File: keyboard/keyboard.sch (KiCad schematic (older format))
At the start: 23 parts, among them J1 Mini-DIN-6, J2 Conn_01x13, U1 74HC595, U2 74HC595, U3 74HC180, U4 74HC08, U5 74HC14

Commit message: Update keyboard
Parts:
- added C8: 1uF, Capacitor_THT:CP_Radial_D4.0mm_P2.00mm, symbol Device:CP
- H1, H2, H3, H4: footprint MountingHole:MountingHole_2.7mm_M2.5_Pad -> MountingHole:MountingHole_3.2mm_M3_Pad
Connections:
- net GND: now also C8.2
- net VCC: now also C8.1
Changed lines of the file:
@@
 F 0 "H1" V 9704 2450 50  0000 L CNN
 F 1 "MountingHole_Pad" V 9795 2450 50  0000 L CNN
-F 2 "MountingHole:MountingHole_2.7mm_M2.5_Pad" H 9750 2300 50  0001 C CNN
+F 2 "MountingHole:MountingHole_3.2mm_M3_Pad" H 9750 2300 50  0001 C CNN
 F 3 "~" H 9750 2300 50  0001 C CNN
 	1    9750 2300
@@
 F 0 "H2" V 9704 2650 50  0000 L CNN
 F 1 "MountingHole_Pad" V 9795 2650 50  0000 L CNN
-F 2 "MountingHole:MountingHole_2.7mm_M2.5_Pad" H 9750 2500 50  0001 C CNN
+F 2 "MountingHole:MountingHole_3.2mm_M3_Pad" H 9750 2500 50  0001 C CNN
 F 3 "~" H 9750 2500 50  0001 C CNN
 	1    9750 2500
@@
 F 0 "H3" V 9704 2850 50  0000 L CNN
 F 1 "MountingHole_Pad" V 9795 2850 50  0000 L CNN
-F 2 "MountingHole:MountingHole_2.7mm_M2.5_Pad" H 9750 2700 50  0001 C CNN
+F 2 "MountingHole:MountingHole_3.2mm_M3_Pad" H 9750 2700 50  0001 C CNN
 F 3 "~" H 9750 2700 50  0001 C CNN
 	1    9750 2700
@@
 F 0 "H4" V 9704 3050 50  0000 L CNN
 F 1 "MountingHole_Pad" V 9795 3050 50  0000 L CNN
-F 2 "MountingHole:MountingHole_2.7mm_M2.5_Pad" H 9750 2900 50  0001 C CNN
+F 2 "MountingHole:MountingHole_3.2mm_M3_Pad" H 9750 2900 50  0001 C CNN
 F 3 "~" H 9750 2900 50  0001 C CNN
 	1    9750 2900
@@
 	1    0    0    -1
 $EndComp
+$Comp
+L Device:CP C8
+U 1 1 60B22BE5
+P 4050 7150
+F 0 "C8" H 4168 7196 50  0000 L CNN
+F 1 "1uF" H 4168 7105 50  0000 L CNN
+F 2 "Capacitor_THT:CP_Radial_D4.0mm_P2.00mm" H 4088 7000 50  0001 C CNN
+F 3 "~" H 4050 7150 50  0001 C CNN
+	1    4050 7150
+	1    0    0    -1
+$EndComp
+Wire Wire Line
+	3550 7000 4050 7000
+Connection ~ 3550 7000
+Wire Wire Line
+	4050 7300 3550 7300
+Connection ~ 3550 7300
 Wire Bus Line
 	4900 5150 6800 5150

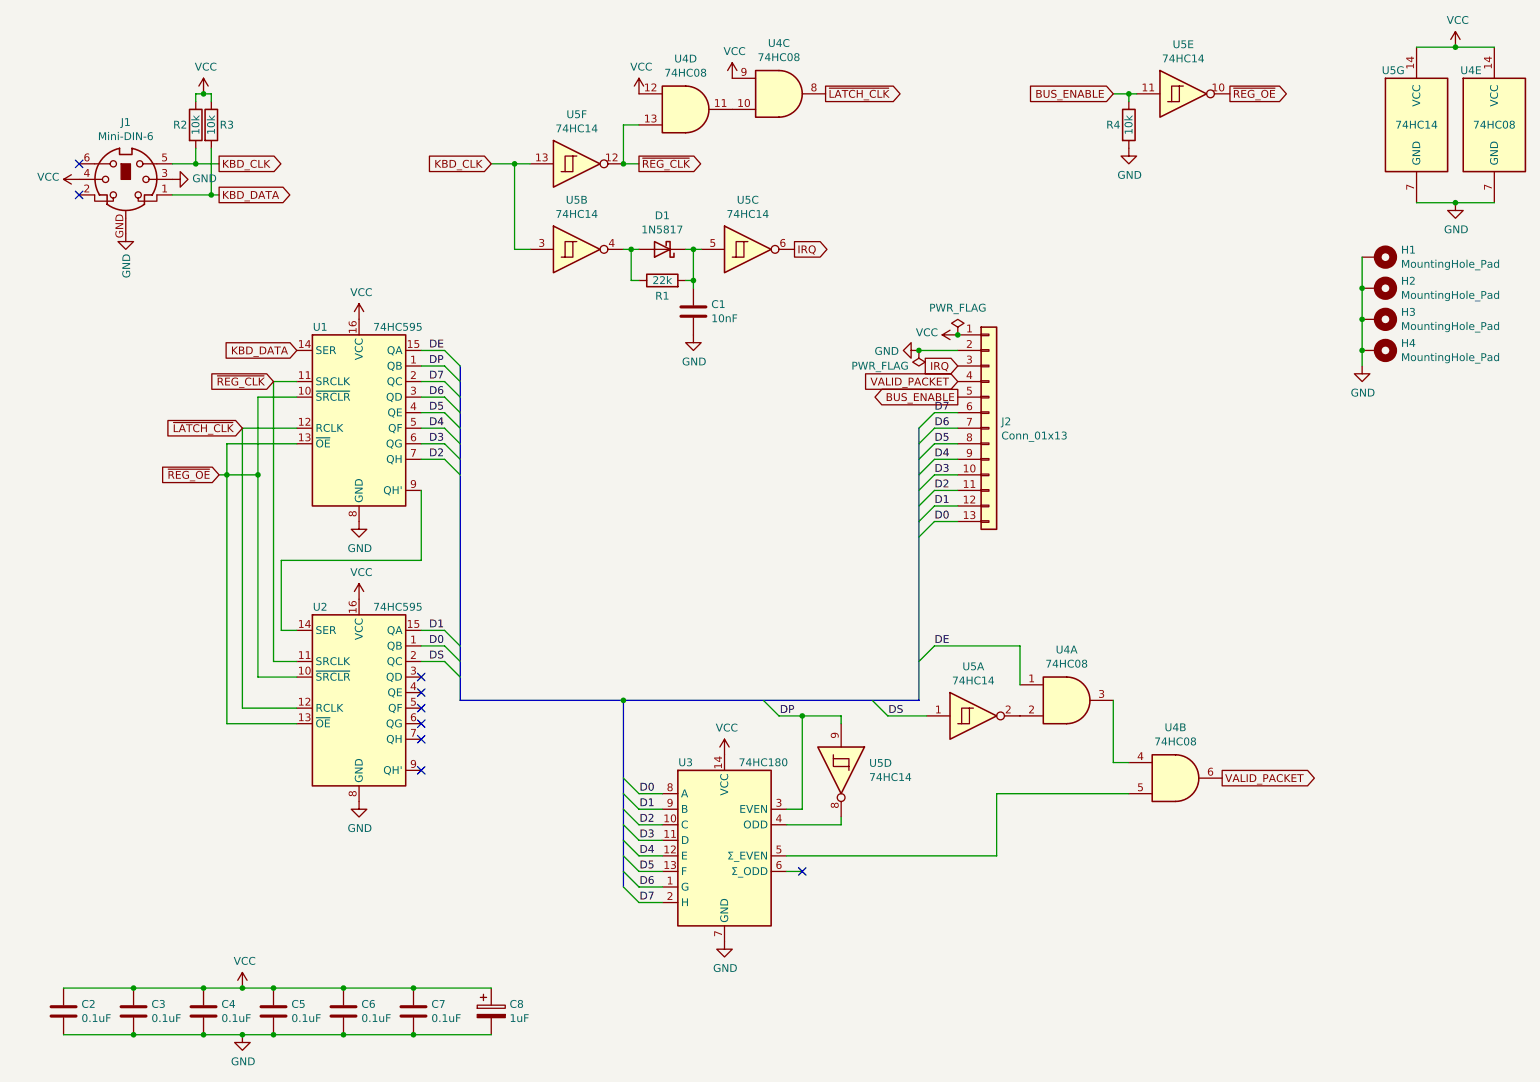
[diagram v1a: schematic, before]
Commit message: Updated keyboard
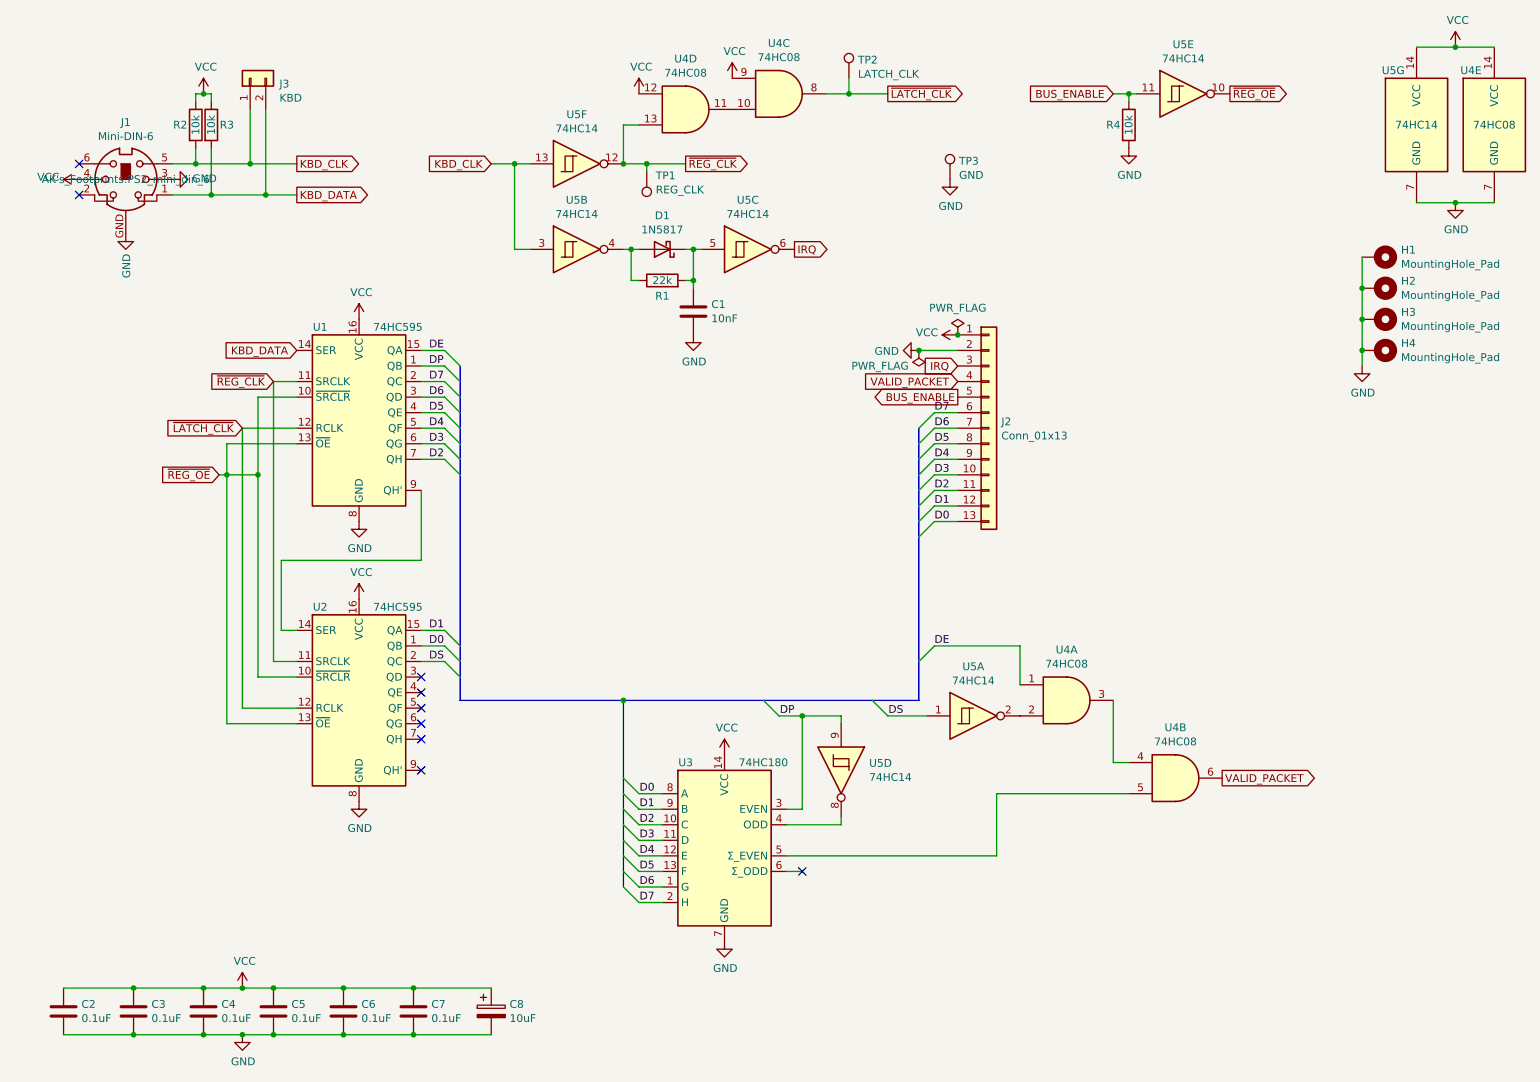
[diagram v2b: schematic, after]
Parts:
- added J3: KBD, Connector_PinHeader_2.54mm:PinHeader_1x02_P2.54mm_Vertical, symbol Connector_Generic:Conn_01x02
- added TP1: REG_CLK, TestPoint:TestPoint_Loop_D2.60mm_Drill1.6mm_Beaded, symbol Connector:TestPoint
- added TP2: LATCH_CLK, TestPoint:TestPoint_Loop_D2.60mm_Drill1.6mm_Beaded, symbol Connector:TestPoint
- added TP3: GND, TestPoint:TestPoint_Loop_D2.60mm_Drill1.6mm_Beaded, symbol Connector:TestPoint
- C8: value 1uF -> 10uF
- J1: footprint AK's_Footprints:Mini_din6 -> AK's_Footprints:PS2_mini_din_6
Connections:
- net GND: now also TP3.1
- net KBD_CLK: now also J3.1 (Pin_1)
- net KBD_DATA: now also J3.2 (Pin_2)
- net ~LATCH_CLK: now also TP2.1
- net ~REG_CLK: now also TP1.1
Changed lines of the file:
@@
 F 0 "J1" H 1700 2167 50  0000 C CNN
 F 1 "Mini-DIN-6" H 1700 2076 50  0000 C CNN
-F 2 "AK's_Footprints:Mini_din6" H 1700 1800 50  0001 C CNN
+F 2 "AK's_Footprints:PS2_mini_din_6" H 1700 1800 50  0000 C CNN
 F 3 "http://service.powerdynamics.com/ec/Catalog17/Section%2011.pdf" H 1700 1800 50  0001 C CNN
 	1    1700 1800
 	1    0    0    -1
 $EndComp
-Text GLabel 2300 1900 2    50   Output ~ 0
+Text GLabel 2800 1900 2    50   Output ~ 0
 KBD_DATA
-Text GLabel 2300 1700 2    50   Output ~ 0
+Text GLabel 2800 1700 2    50   Output ~ 0
 KBD_CLK
 $Comp
@@
 Text GLabel 4050 1700 0    50   Input ~ 0
 KBD_CLK
-Text GLabel 5000 1700 2    50   Output ~ 0
+Text GLabel 5300 1700 2    50   Output ~ 0
 ~REG_CLK
 Text GLabel 2650 3100 0    50   Input ~ 0
@@
 Wire Wire Line
 	4900 1700 4900 1450
-Wire Wire Line
-	4900 1700 5000 1700
 Connection ~ 4900 1700
 $Comp
@@
 	1    0    0    -1
 $EndComp
-Text GLabel 6200 1250 2    50   Output ~ 0
+Text GLabel 6600 1250 2    50   Output ~ 0
 ~LATCH_CLK
 Text GLabel 2450 3400 0    50   Input ~ 0
@@
 Connection ~ 2150 1700
 Wire Wire Line
-	2150 1700 2300 1700
+	2150 1700 2500 1700
 $Comp
 L Device:R R2
@@
 	2000 1900 2250 1900
 Connection ~ 2250 1900
-Wire Wire Line
-	2250 1900 2300 1900
 $Comp
 L power:VCC #PWR0101
@@
 P 4050 7150
 F 0 "C8" H 4168 7196 50  0000 L CNN
-F 1 "1uF" H 4168 7105 50  0000 L CNN
+F 1 "10uF" H 4168 7105 50  0000 L CNN
 F 2 "Capacitor_THT:CP_Radial_D4.0mm_P2.00mm" H 4088 7000 50  0001 C CNN
 F 3 "~" H 4050 7150 50  0001 C CNN
@@
 	4050 7300 3550 7300
 Connection ~ 3550 7300
+Connection ~ 2500 1700
+Wire Wire Line
+	2500 1700 2800 1700
+$Comp
+L Connector:TestPoint TP2
+U 1 1 6193978F
+P 6350 1150
+F 0 "TP2" H 6408 1268 50  0000 L CNN
+F 1 "LATCH_CLK" H 6408 1177 50  0000 L CNN
+F 2 "TestPoint:TestPoint_Loop_D2.60mm_Drill1.6mm_Beaded" H 6550 1150 50  0001 C CNN
+F 3 "~" H 6550 1150 50  0001 C CNN
+	1    6350 1150
+	1    0    0    -1
+$EndComp
+Wire Wire Line
+	4900 1700 5050 1700
+$Comp
+L Connector:TestPoint TP1
+U 1 1 6193AD45
+P 5050 1750
+F 0 "TP1" H 4992 1776 50  0000 R CNN
+F 1 "REG_CLK" H 4992 1867 50  0000 R CNN
+F 2 "TestPoint:TestPoint_Loop_D2.60mm_Drill1.6mm_Beaded" H 5250 1750 50  0001 C CNN
+F 3 "~" H 5250 1750 50  0001 C CNN
+	1    5050 1750
+	-1   0    0    1
+$EndComp
+Wire Wire Line
+	6200 1250 6350 1250
+Wire Wire Line
+	6350 1150 6350 1250
+Connection ~ 6350 1250
+Wire Wire Line
+	6350 1250 6600 1250
+Wire Wire Line
+	5050 1750 5050 1700
+Connection ~ 5050 1700
+Wire Wire Line
+	5050 1700 5300 1700
+$Comp
+L Connector:TestPoint TP3
+U 1 1 6194C173
+P 7000 1800
+F 0 "TP3" H 7058 1918 50  0000 L CNN
+F 1 "GND" H 7058 1827 50  0000 L CNN
+F 2 "TestPoint:TestPoint_Loop_D2.60mm_Drill1.6mm_Beaded" H 7200 1800 50  0001 C CNN
+F 3 "~" H 7200 1800 50  0001 C CNN
+	1    7000 1800
+	1    0    0    -1
+$EndComp
+$Comp
+L power:GND #PWR0106
+U 1 1 6194C5AC
+P 7000 1800
+F 0 "#PWR0106" H 7000 1550 50  0001 C CNN
+F 1 "GND" H 7005 1627 50  0000 C CNN
+F 2 "" H 7000 1800 50  0001 C CNN
+F 3 "" H 7000 1800 50  0001 C CNN
+	1    7000 1800
+	1    0    0    -1
+$EndComp
+$Comp
+L Connector_Generic:Conn_01x02 J3
+U 1 1 619635EB
+P 2500 1150
+F 0 "J3" V 2464 962 50  0000 R CNN
+F 1 "KBD" V 2373 962 50  0000 R CNN
+F 2 "Connector_PinHeader_2.54mm:PinHeader_1x02_P2.54mm_Vertical" H 2500 1150 50  0001 C CNN
+F 3 "~" H 2500 1150 50  0001 C CNN
+	1    2500 1150
+	0    -1   -1   0
+$EndComp
+Wire Wire Line
+	2500 1350 2500 1700
+Wire Wire Line
+	2250 1900 2600 1900
+Wire Wire Line
+	2600 1350 2600 1900
 Wire Bus Line
 	4900 5150 6800 5150
@@
 Wire Bus Line
 	3850 3000 3850 5150
+Connection ~ 2600 1900
+Wire Wire Line
+	2600 1900 2800 1900
 $EndSCHEMATC
